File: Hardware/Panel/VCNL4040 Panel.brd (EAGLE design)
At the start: 102.4 x 80.3 mm, 240 parts, among them U1 VCNL4040, U10 VCNL4040, U11 VCNL4040, U12 VCNL4040, U13 VCNL4040, U14 VCNL4040, U15 VCNL4040, U16 VCNL4040, U17 VCNL4040, U18 VCNL4040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

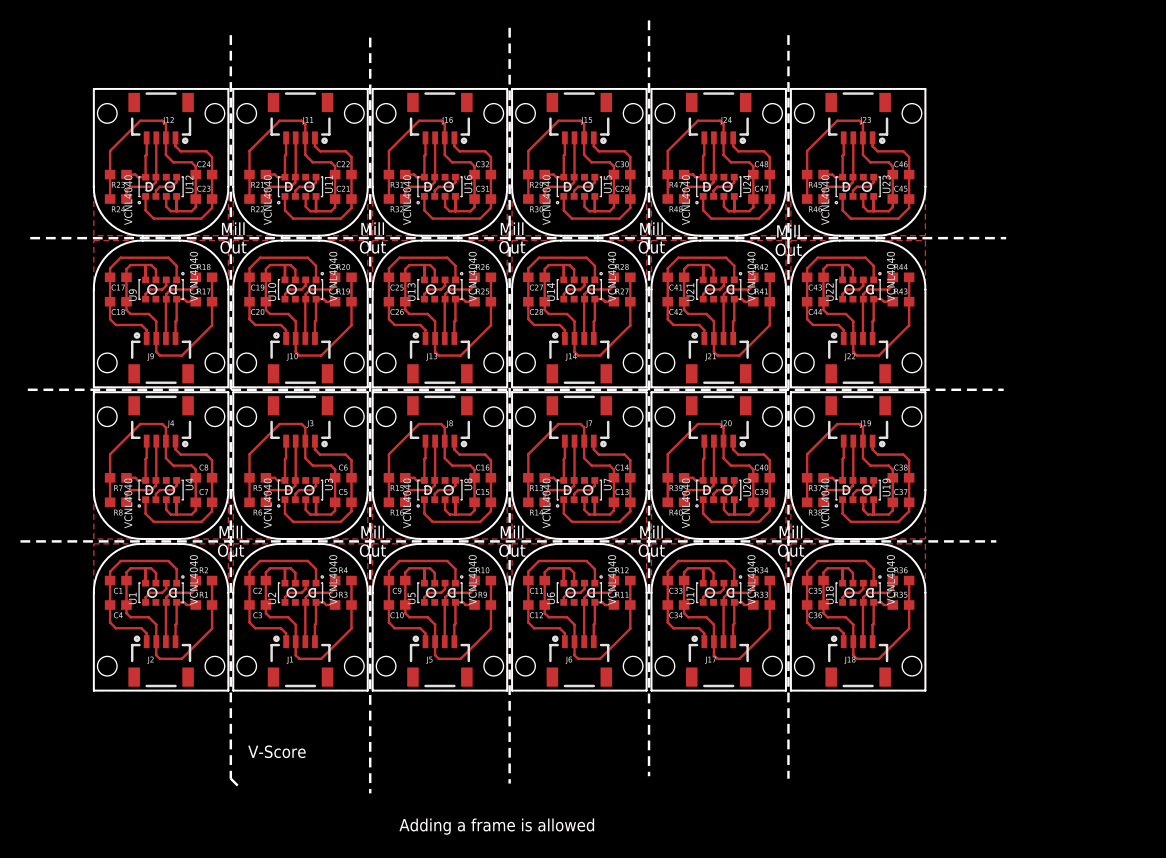
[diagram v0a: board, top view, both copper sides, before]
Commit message: New panel with silk indicators on pins.
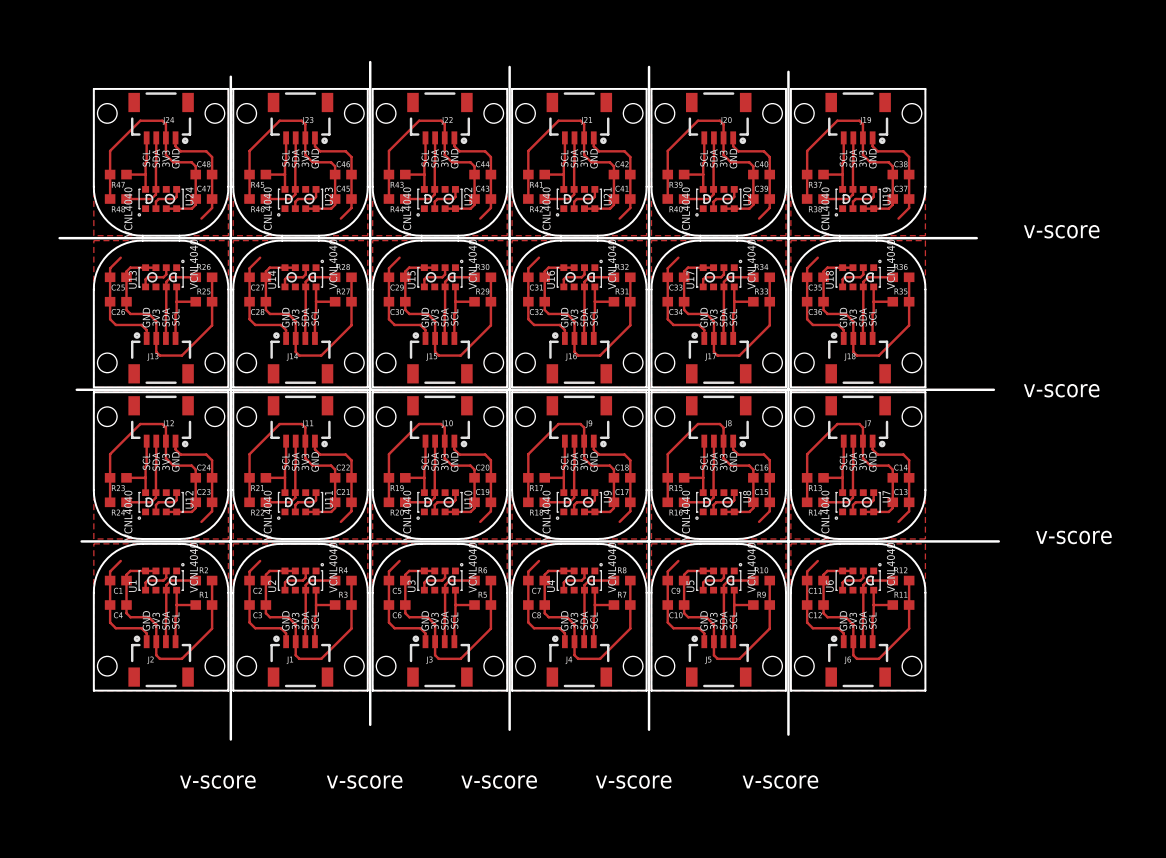
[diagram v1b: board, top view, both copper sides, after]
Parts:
- moved U$16 60.4 mm to (56.0, 2.54), turned to 0 degrees
- moved U$88 60.4 mm to (30.4, 59.9), turned to 180 degrees
- moved U$93 57.9 mm to (6.99, 51.1)
- moved U24 57.9 mm to (6.99, 51.1)
- moved U$89 57.9 mm to (21.5, 51.1)
- moved U23 57.9 mm to (21.5, 51.1)
- moved J24 57.9 mm to (6.99, 57.4)
- moved R45 57.9 mm to (17.0, 53.6)
- moved R46 57.9 mm to (17.0, 51.1)
- moved U$92 57.9 mm to (15.9, 59.9)
- moved U$94 57.9 mm to (6.99, 61.2)
- moved C47 57.9 mm to (11.4, 51.1)
- moved C48 57.9 mm to (11.4, 53.6)
- moved J23 57.9 mm to (21.5, 57.4)
- moved R47 57.9 mm to (2.54, 53.6)
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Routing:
- net GND15: track 19.6 -> 12.0 mm
- net GND3: track 19.6 -> 12.0 mm
- net GND14: track 19.6 -> 12.0 mm
- net GND9: track 19.6 -> 12.0 mm
- net GND16: track 19.6 -> 12.0 mm
- net GND1: track 19.6 -> 12.0 mm
- net GND7: track 19.6 -> 12.0 mm
- net GND22: track 19.6 -> 12.0 mm
- net GND20: track 19.6 -> 12.0 mm
- net GND17: track 19.6 -> 12.0 mm
- net GND12: track 19.6 -> 12.0 mm
- net GND10: track 19.6 -> 12.0 mm
- net GND11: track 19.6 -> 12.0 mm
- net GND8: track 19.6 -> 12.0 mm
- net GND6: track 19.6 -> 12.0 mm
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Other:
- board size 102.4 x 80.3 mm -> 97.5 x 70.4 mm
- board text added: "3V3"
- board text added: "GND"
- board text added: "SCL"
- board text added: "SDA"
- board text added: "v-score"
- board text removed: "Adding a frame is allowed"
- board text removed: "Mill Out"
- board text removed: "V-Score"
